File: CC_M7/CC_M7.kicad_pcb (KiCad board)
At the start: 4 copper layers, 40 x 65 mm, 127 parts, among them J1 Conn_01x04_Pin, J10 Conn_01x04_Pin, J11 USB_B_Micro, J12 Conn_01x04_Pin, J13 Batt_Pins, J3 Conn_01x03_Pin, J4 Conn_01x03_Pin, J5 Conn_01x03_Pin, J6 Conn_01x03_Pin, J7 Conn_01x03_Pin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

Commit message: PCB track draw.
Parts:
- removed D2: LED, LED_SMD:LED_0603_1608Metric
- removed R7: 1.5k, Resistor_SMD:R_0603_1608Metric
- added F1: Polyfuse, Fuse:Fuse_1206_3216Metric, F.Cu at (101.0, 166.2)
- C34, C41, C42, R15: moved to B.Cu
- C43, C57: footprint Capacitor_SMD:C_0805_2012Metric -> Capacitor_SMD:C_1206_3216Metric; moved to F.Cu
- C47: footprint Capacitor_SMD:C_0603_1608Metric -> Capacitor_SMD:C_1206_3216Metric; moved to F.Cu
- C56, R3: moved to F.Cu
- D1: value LED -> MBR230LSFT1G; footprint LED_SMD:LED_0603_1608Metric -> MBR230LSFT1G:SODFL3619X98N; moved to B.Cu
- J13: footprint Connector_Molex:Molex_KK-254_AE-6410-02A_1x02_P2.54mm_Vertical -> Connector_PinSocket_2.54mm:PinSocket_1x02_P2.54mm_Vertical
- JP1, JP2, JP3, JP4, JP5, JP6, JP7, JP8: footprint Capacitor_SMD:C_0201_0603Metric -> Jumper:SolderJumper-2_P1.3mm_Open_TrianglePad1.0x1.5mm
- R6: value 1.5k -> 10k
- moved D1 37.4 mm to (121.0, 164.5)
- moved C19 33.4 mm to (112.2, 148.7), turned to -90 degrees
- moved S1 31.2 mm to (114.3, 148.6), turned to 0 degrees
- moved J13 26.2 mm to (123.9, 165.6), turned to 180 degrees
- moved C43 25.4 mm to (119.9, 166.6), turned to 180 degrees
- moved C57 25.3 mm to (119.9, 161.8), turned to 180 degrees
- moved U8 24.1 mm to (114.8, 169.3), turned to 0 degrees
- moved R10 23.2 mm to (118.1, 167.3), turned to 180 degrees
- moved U2 19.7 mm to (96.2, 130.3), turned to -90 degrees
- moved R13 19.1 mm to (118.1, 165.7), turned to 0 degrees
- moved C48 18.3 mm to (118.1, 164.2), turned to 180 degrees
- moved R12 15.8 mm to (118.1, 161.2), turned to 180 degrees
- moved C49 15.8 mm to (118.1, 162.7), turned to 0 degrees
- moved C47 15.8 mm to (119.9, 164.2), turned to 180 degrees
- moved C22 10.2 mm to (100.4, 147.9)
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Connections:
- C43 pad 2: +BATT -> Net-(U8-VIN)
- C47 pad 2: +BATT -> Net-(U8-VIN)
- C56 pad 2: Net-(C56-Pad2) -> VIN_5V
- C57 pad 2: +BATT -> Net-(U8-VIN)
- D3 pad 2: LED2 -> LED1
- D4 pad 2: LED3 -> LED0
- J1 pad 1: +BATT -> VIN_5V
- L3 pad 2: Net-(C56-Pad2) -> VIN_5V
- R10 pad 2: +BATT -> Net-(U8-VIN)
- R12 pad 1: Net-(C56-Pad2) -> VIN_5V
- R6 pad 1: GND -> BOOT0
- R6 pad 2: Net-(D1-K) -> GND
- U1 pad 40: LED2 -> LED0
- U1 pad 41: LED3 -> LED1
- U1 pad 84: LED0 -> unconnected-(U1-PD3-Pad84)
- U1 pad 85: LED1 -> unconnected-(U1-PD4-Pad85)
- U1 pad 94: unconnected-(U1-BOOT0-Pad94) -> BOOT0
- U8 pad 1: +BATT -> Net-(U8-VIN)
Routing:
- net I2C1_SDA: track 0.00 -> 61.3 mm, vias 0 -> 2
- net I2C1_SCL: track 0.00 -> 60.3 mm, vias 0 -> 2
- net UART4_RX: track 0.00 -> 31.6 mm, vias 0 -> 2
- net UART4_TX: track 0.00 -> 28.2 mm, vias 0 -> 2
- net UART1_RX: track 0.00 -> 24.7 mm, vias 0 -> 1
- net UART1_TX: track 0.00 -> 23.6 mm, vias 0 -> 1
- net +5V: track 0.00 -> 23.5 mm, vias 0 -> 2
- net +3.3V: track 0.00 -> 17.1 mm, vias 0 -> 6
- net PC15: track 0.00 -> 16.1 mm, vias 0 -> 2
- net J2_32: track 0.00 -> 16.1 mm, vias 0 -> 1
- net UART3_RX: track 0.00 -> 14.3 mm, vias 0 -> 2
- net PC14: track 0.00 -> 14.0 mm, vias 0 -> 1
- net PC13: track 0.00 -> 13.7 mm, vias 0 -> 1
- net UART3_TX: track 0.00 -> 13.5 mm, vias 0 -> 2
- net PE2: track 0.00 -> 13.3 mm, vias 0 -> 2
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- added copper zone on B.Cu, net GND
- added copper zone on F.Cu, net GND
- added copper zone on In1.Cu, net GND
- removed copper zone on In2.Cu, net +3.3V

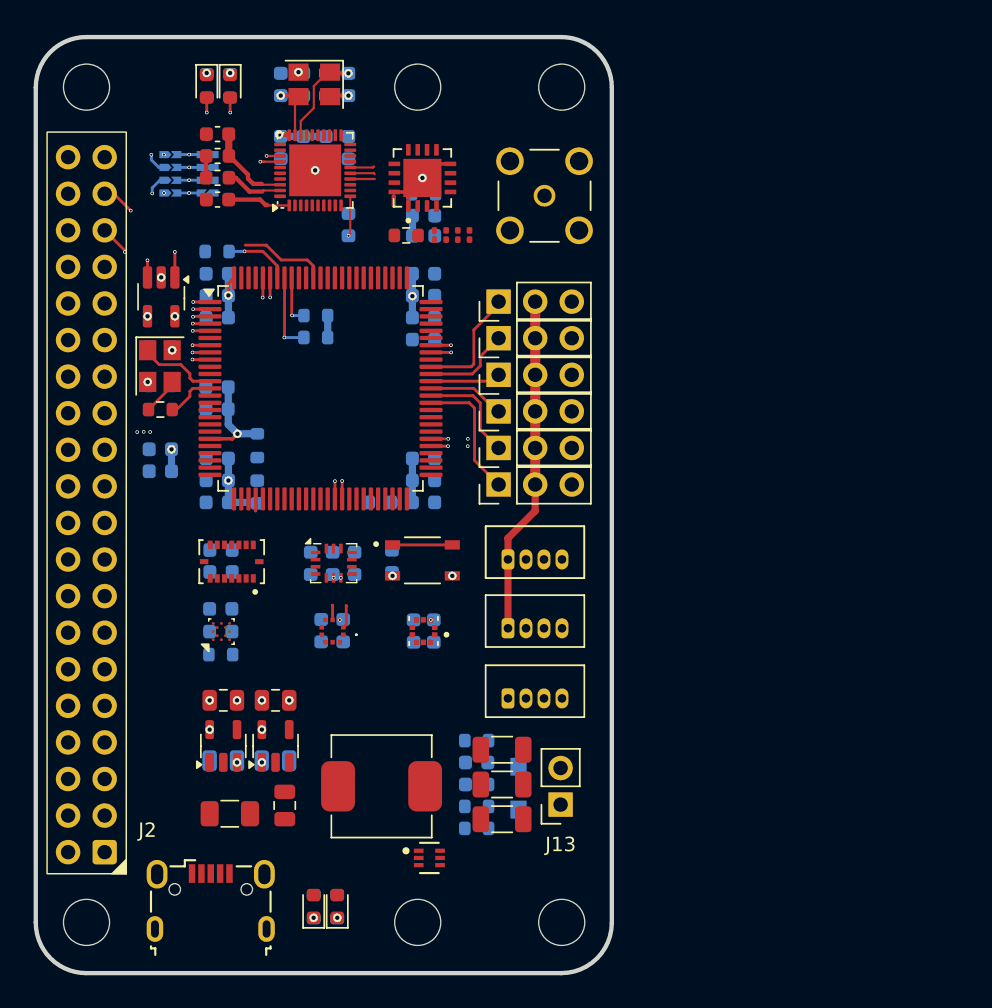
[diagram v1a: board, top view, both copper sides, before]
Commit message: Reverse current protection added. | Routing progress.
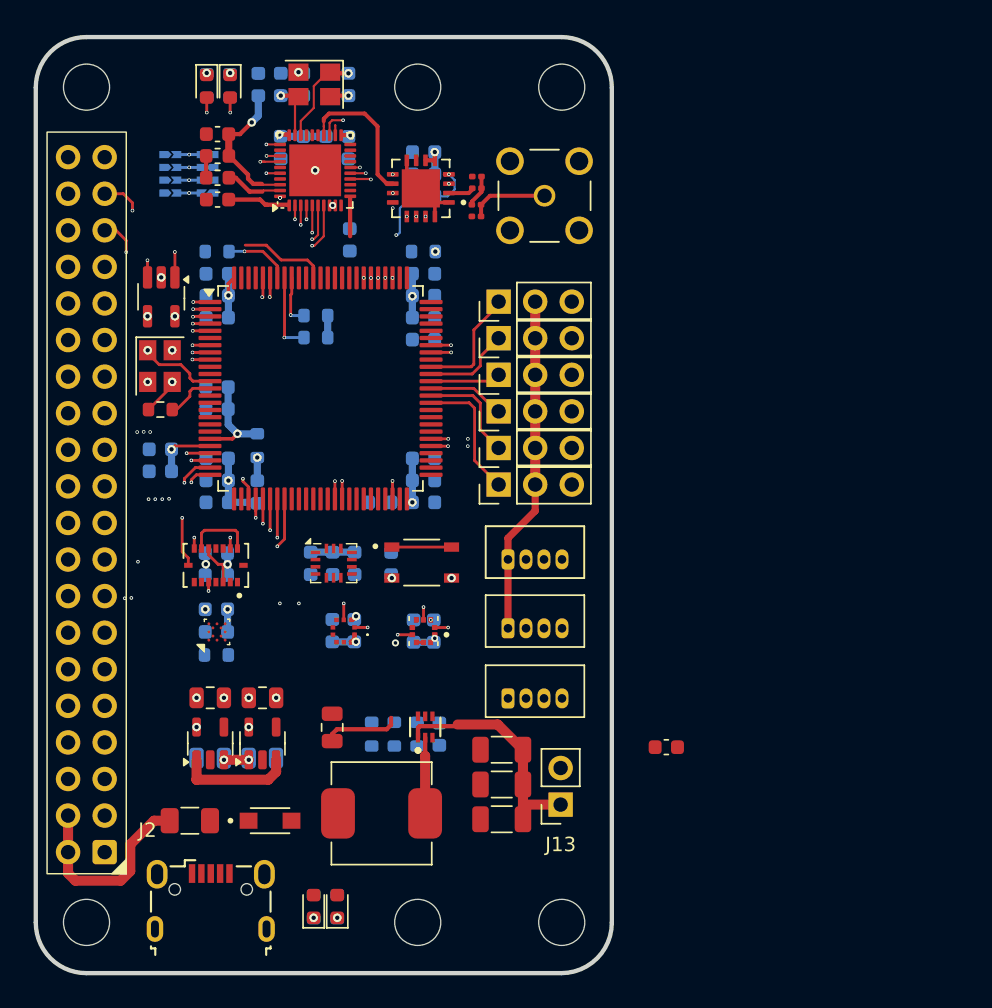
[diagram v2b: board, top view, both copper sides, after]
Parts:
- C49, D1: moved to F.Cu
- R16: moved to B.Cu
- moved D1 17.4 mm to (103.8, 166.7), turned to 0 degrees
- moved C49 13.2 mm to (131.3, 161.6), turned to 180 degrees
- moved U8 9.10 mm to (114.5, 160.2), turned to 90 degrees
- moved R10 7.74 mm to (114.0, 160.7), turned to -90 degrees
- moved R13 7.60 mm to (112.4, 160.7), turned to 90 degrees
- moved R12 7.30 mm to (110.8, 160.7), turned to -90 degrees
- moved C56 6.34 mm to (108.1, 160.2), turned to -90 degrees
- moved C43 4.83 mm to (119.9, 161.8), turned to 0 degrees
- moved C57 4.83 mm to (119.9, 166.6), turned to 0 degrees
- moved C37 4.69 mm to (102.9, 115.6)
- moved C28 4.59 mm to (118.1, 122.0), turned to 180 degrees
- moved C41 4.42 mm to (114.4, 120.3), turned to 180 degrees
- moved L6 4.39 mm to (118.1, 122.8), turned to 0 degrees
- moved C48 4.35 mm to (115.5, 160.7), turned to 90 degrees
- moved C42 4.27 mm to (114.4, 121.8), turned to 180 degrees
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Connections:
- C43 pad 2: Net-(U8-VIN) -> +BATT
- C47 pad 2: Net-(U8-VIN) -> +BATT
- C56 pad 2: VIN_5V -> Net-(C56-Pad2)
- C57 pad 2: Net-(U8-VIN) -> +BATT
- D1 pad A: +BATT -> Net-(C56-Pad2)
- D1 pad K: Net-(U8-VIN) -> VIN_5V
- L3 pad 2: VIN_5V -> Net-(C56-Pad2)
- R10 pad 2: Net-(U8-VIN) -> +BATT
- R12 pad 1: VIN_5V -> Net-(C56-Pad2)
- U8 pad 1: Net-(U8-VIN) -> +BATT
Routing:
- net 3V3_RF: track 5.22 -> 65.5 mm, vias 3 -> 7
- net PA4: track 0.00 -> 27.9 mm, vias 0 -> 2
- net UART2_RX: track 0.00 -> 24.3 mm, vias 0 -> 2
- net +5V: track 23.5 -> 47.3 mm
- net UART2_TX: track 0.00 -> 22.8 mm, vias 0 -> 2
- net PA1: track 0.00 -> 18.4 mm, vias 0 -> 3
- net SPI1_MISO: track 4.37 -> 21.4 mm, vias 0 -> 1
- net PA0: track 4.34 -> 21.0 mm, vias 0 -> 3
- net +BATT: track 0.00 -> 16.2 mm
- net +3.3V: track 17.1 -> 31.3 mm, vias 6 -> 11
- net NRF_SPI0_CS: track 0.00 -> 13.2 mm, vias 0 -> 2
- net SPI1_SCK: track 7.09 -> 19.7 mm, vias 0 -> 2
- net SPI1_MOSI: track 3.52 -> 15.5 mm, vias 0 -> 2
- net NRF_PA_PDN: track 0.00 -> 11.9 mm, vias 0 -> 2
- net I2C2_SDA: track 0.00 -> 11.5 mm
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
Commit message: Routing Progress | BMM150 removed.
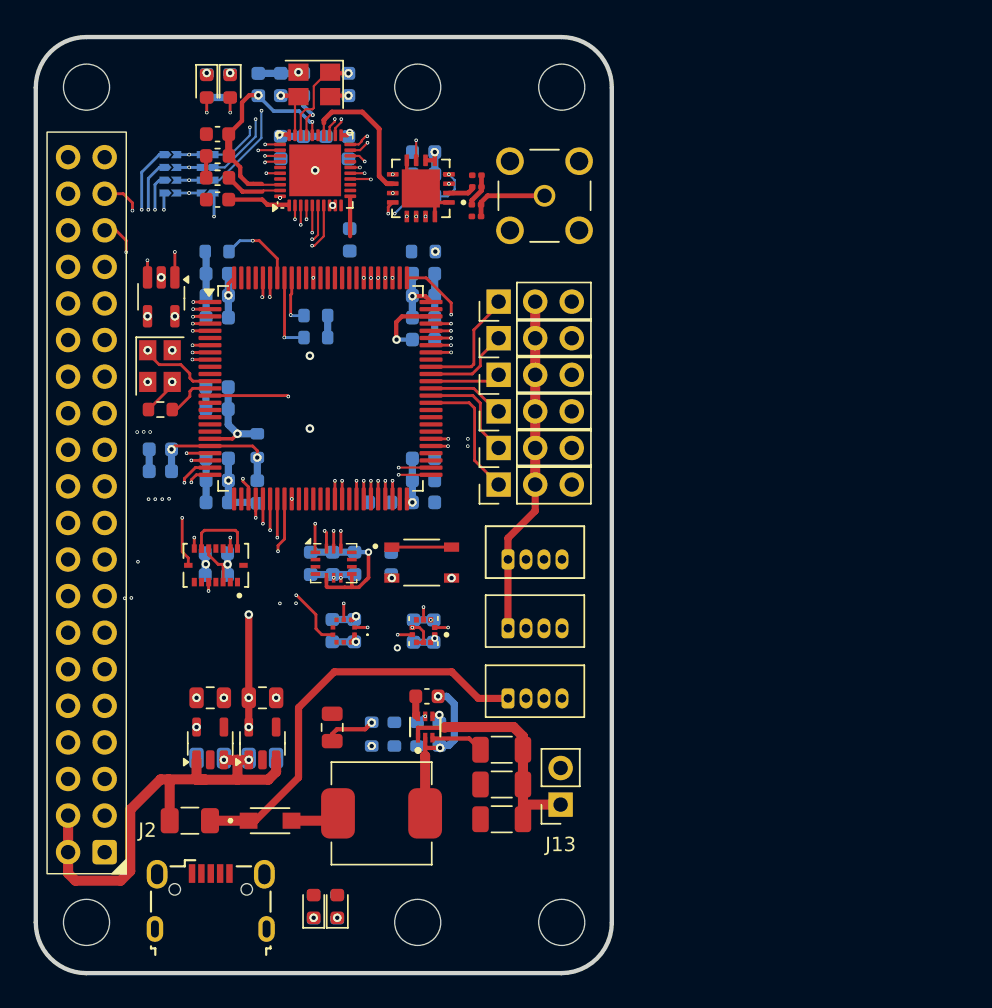
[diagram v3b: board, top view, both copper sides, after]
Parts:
- removed C26, C27: 100nF, Capacitor_SMD:C_0603_1608Metric
- removed R11: 1k, Resistor_SMD:R_0603_1608Metric
- removed U5: BMM150, Package_CSP:WLCSP-12_1.56x1.56mm_P0.4mm
- moved C49 17.0 mm to (114.7, 158.1), turned to 0 degrees
- moved C28 0.09 mm to (118.1, 121.9)
- moved L6 0.09 mm to (118.1, 122.7)
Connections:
- U12 pad 13: unconnected-(U12-AP_SCL/AP_SCLK-Pad13) -> SPI1_SCK
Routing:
- net +5V: track 47.3 -> 82.8 mm
- net GND: track 7.94 -> 40.8 mm, vias 16 -> 18
- net SWCLK: track 0.00 -> 31.6 mm, vias 0 -> 2
- net NRST: track 4.15 -> 34.9 mm, vias 0 -> 2
- net SWDIO: track 0.00 -> 30.1 mm, vias 0 -> 2
- net VIN_5V: track 0.00 -> 28.6 mm
- net NRF_SWCLK: track 0.00 -> 16.4 mm, vias 0 -> 2
- net I2C1_IRQ1: track 0.00 -> 15.5 mm, vias 0 -> 2
- net NRF_SWDIO: track 0.00 -> 15.3 mm, vias 0 -> 2
- net I2C1_IRQ3: track 1.02 -> 13.9 mm, vias 1 -> 2
- net NRF_PA_MODE: track 3.18 -> 15.6 mm, vias 1 -> 2
- net NRF_PA_RX_EN: track 0.70 -> 10.0 mm, vias 0 -> 2
- net +3.3V: track 31.3 -> 39.0 mm
- net SWO: track 6.16 -> 13.7 mm, vias 0 -> 2
- net 3V3_RF: track 65.5 -> 72.9 mm, vias 7 -> 12
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
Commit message: Routing | Silkscreen Design Completed. | Power Led Added. | Schematic PDF deleted | Mounting Hole Pad Clearance added. | BMM150 Conneciton Fixed.
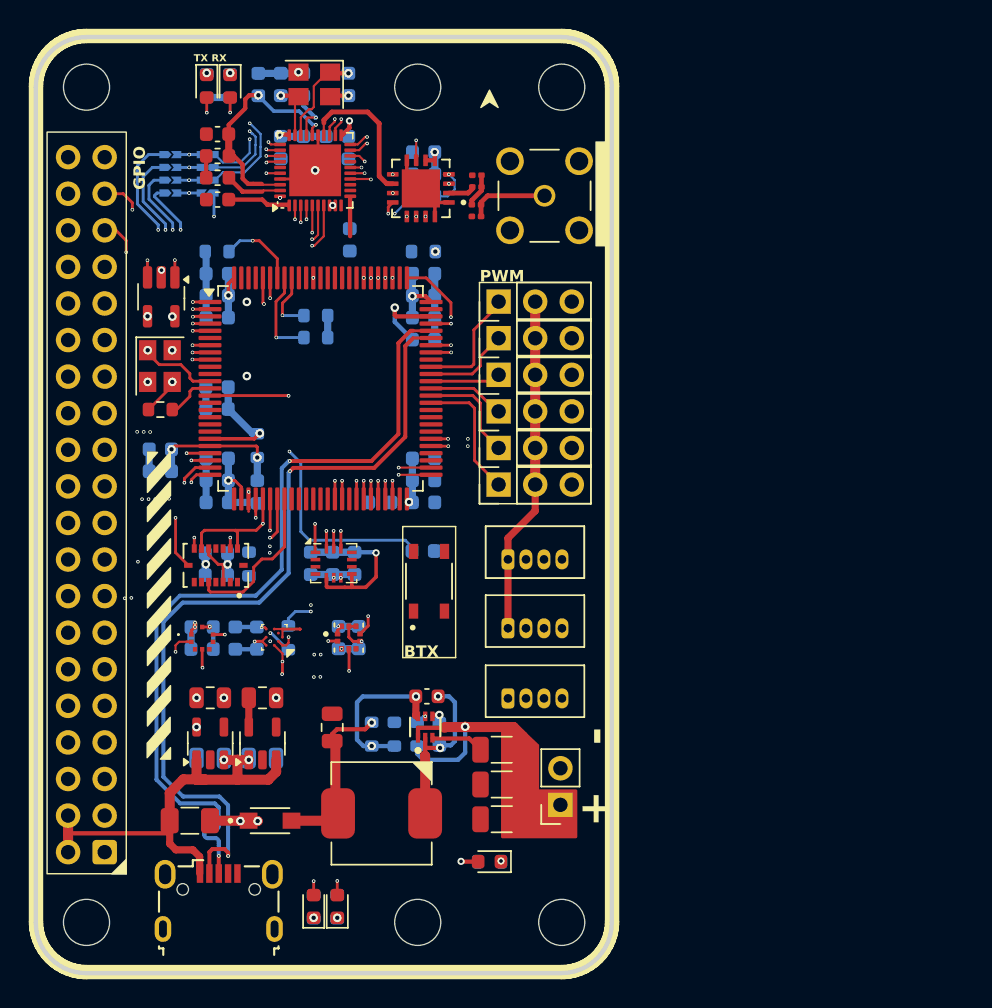
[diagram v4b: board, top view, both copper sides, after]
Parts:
- added C26: 100nF, Capacitor_SMD:C_0603_1608Metric, B.Cu at (102.8, 154.1)
- added C27: 100nF, Capacitor_SMD:C_0603_1608Metric, B.Cu at (101.3, 154.1)
- added D2: LED, LED_SMD:LED_0603_1608Metric, F.Cu at (119.0, 169.6)
- added R11: 1k, Resistor_SMD:R_0603_1608Metric, B.Cu at (105.0, 154.0)
- added R14: 1.5k, Resistor_SMD:R_0603_1608Metric, B.Cu at (119.0, 169.6)
- added R7: 1.5k, Resistor_SMD:R_0603_1608Metric, B.Cu at (102.3, 148.9)
- added U5: BMM150, Package_CSP:WLCSP-12_1.56x1.56mm_P0.4mm, F.Cu at (104.1, 154.0)
- C20, C21, C32, C44: value 12pF -> 16pF
- moved C55 10.6 mm to (99.0, 154.8), turned to 0 degrees
- moved U11 9.84 mm to (99.0, 154.1), turned to 0 degrees
- moved C54 9.05 mm to (99.0, 153.3), turned to 0 degrees
- moved C23 6.63 mm to (108.5, 154.0), turned to -90 degrees
- moved U4 5.21 mm to (109.2, 154.0), turned to 0 degrees
- moved C25 3.84 mm to (109.9, 154.0), turned to -90 degrees
- moved C19 2.39 mm to (114.4, 148.0), turned to 0 degrees
- moved S1 1.39 mm to (114.8, 150.1), turned to 90 degrees
- moved J11 0.56 mm to (100.2, 172.3)
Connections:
- C45 pad 1: +3.3V -> 3V3_RF
- C50 pad 1: 3V3_RF -> +3.3V
- U10 pad 5: 3V3_RF -> +3.3V
- U9 pad 5: +3.3V -> 3V3_RF
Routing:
- net USB_DP: track 1.39 -> 57.6 mm, vias 1 -> 2
- net USB_DM: track 1.39 -> 57.4 mm, vias 1 -> 2
- net LED1: track 1.26 -> 33.8 mm, vias 1 -> 4
- net LED0: track 1.26 -> 33.3 mm, vias 1 -> 4
- net I2C2_SDA: track 11.3 -> 40.6 mm, vias 1 -> 2
- net I2C2_SCL: track 8.74 -> 37.8 mm, vias 1 -> 2
- net NRST: track 34.9 -> 49.2 mm, vias 2 -> 3
- net I2C1_IRQ2: track 1.26 -> 15.5 mm, vias 1 -> 2
- net GND: track 40.8 -> 51.5 mm, vias 18 -> 16
- net Net-(U8-FB): track 1.41 -> 11.1 mm, vias 1 -> 2
- net +3.3V: track 39.0 -> 48.3 mm, vias 11 -> 13
- net +BATT: track 16.6 -> 22.7 mm, vias 0 -> 1
- net I2C1_IRQ1: track 15.5 -> 21.0 mm, vias 2 -> 3
- net Net-(C56-Pad2): track 7.00 -> 12.2 mm
- net I2C1_SCL: track 69.7 -> 74.7 mm, vias 4 -> 6
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- added copper zone on In2.Cu, net +3.3V
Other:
- board text added: "+ -"
- board text added: "1"
- board text added: "15V MAX"
- board text added: "2"
- board text added: "3"
- board text added: "4"
- board text added: "5"
- board text added: "6"
- board text added: "BATT"
- board text added: "BTX"
- board text added: "CCM7"
- board text added: "GNSS"
- board text added: "GPIO"
- board text added: "NRF52"
- board text added: "PWM"
- board text added: "STM32"
- board text added: "TRX"
- board text added: "TX RX"
- board text added: "YENIAY"

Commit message: Small vias replaced big vias
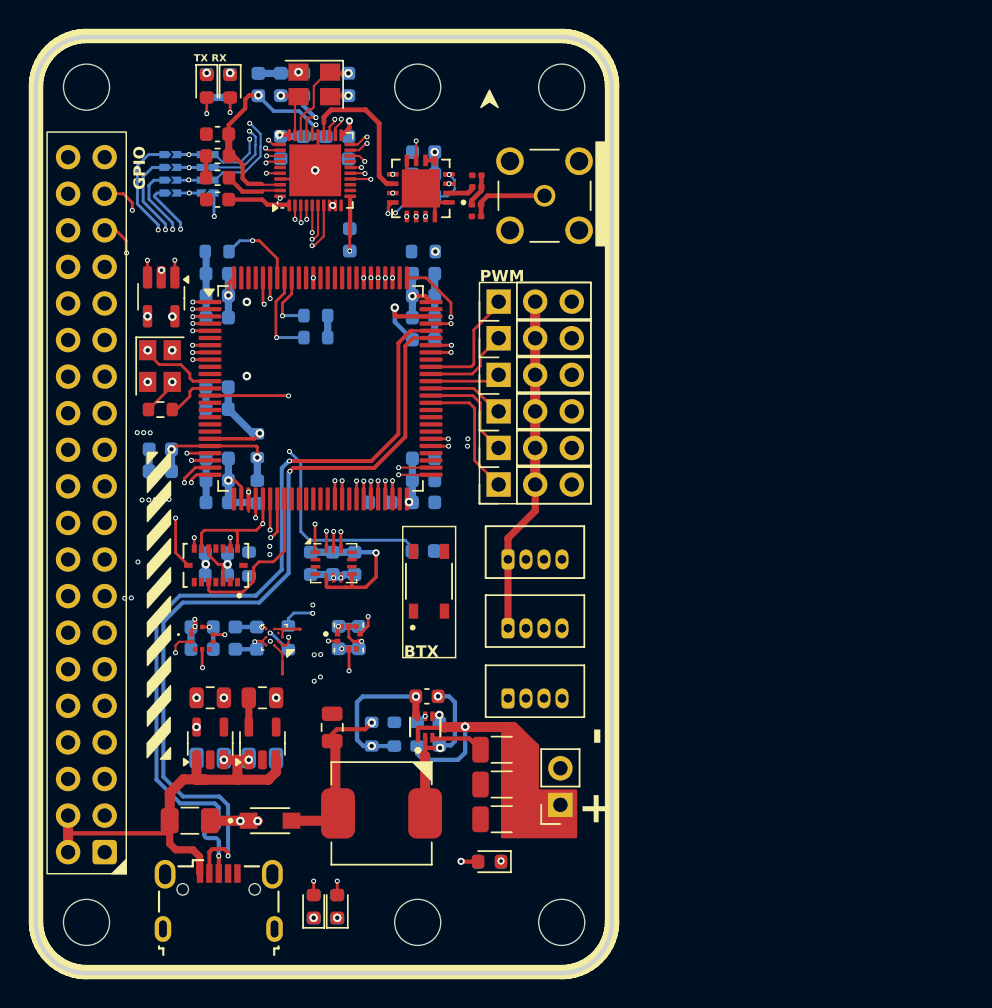
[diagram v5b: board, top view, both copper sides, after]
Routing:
- net USBDEC: track 2.70 -> 3.74 mm, vias 0 -> 1
- net I2C1_SCL: vias 6 -> 4
- net 3V3_RF: vias 11 -> 10
